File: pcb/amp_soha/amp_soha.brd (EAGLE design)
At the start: 90.2 x 48.9 mm, 59 parts, among them IC1 NE5535U, IC2 7812, IC3 7912, Q1 J113, Q2 J113, Q3 J113, Q4 J113

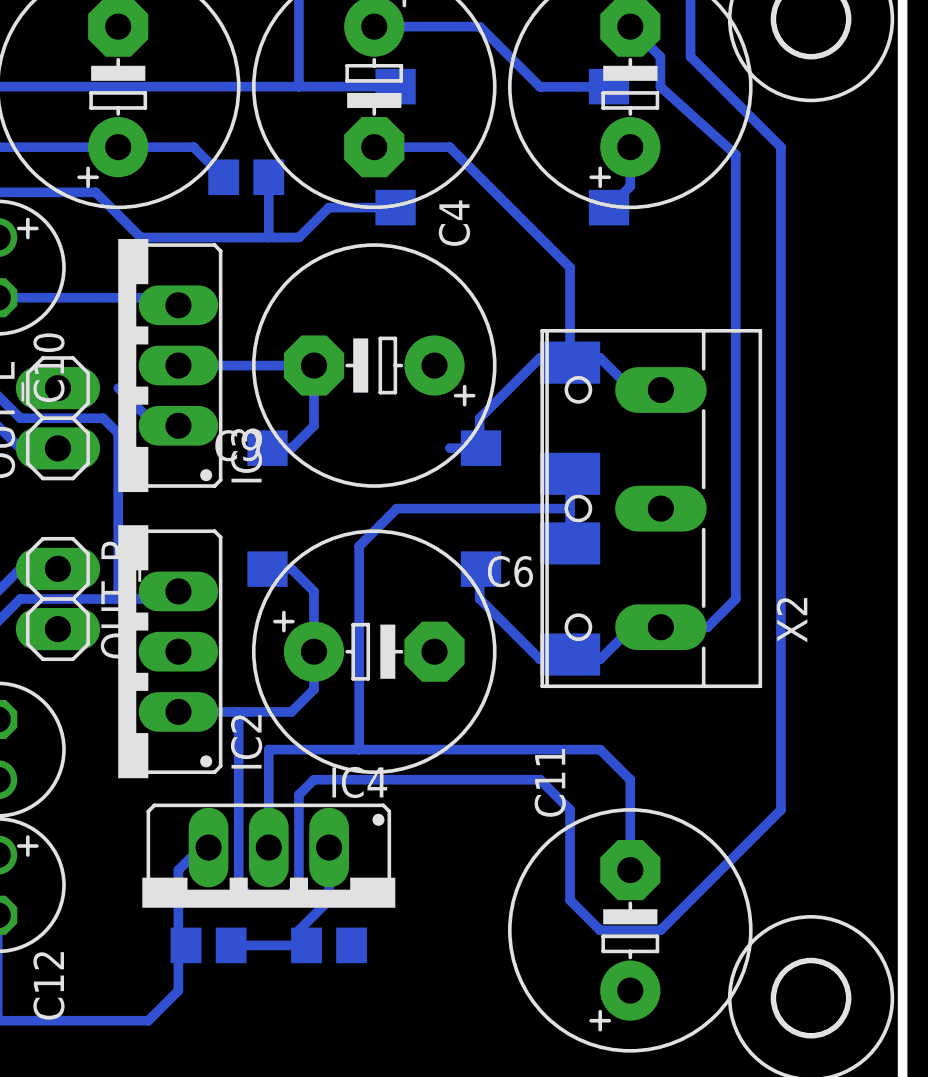
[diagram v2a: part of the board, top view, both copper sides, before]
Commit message: 
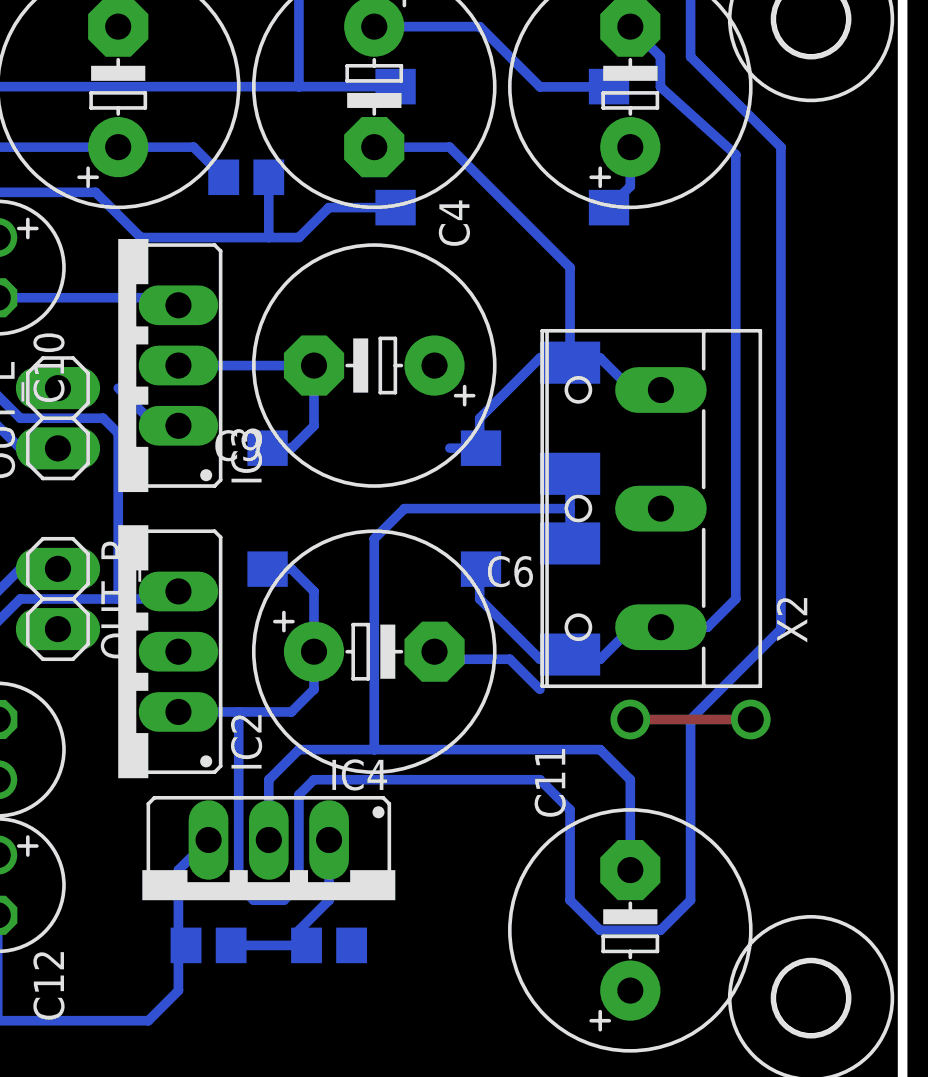
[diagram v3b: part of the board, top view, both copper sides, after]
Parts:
- moved IC4 0.32 mm to (63.5, 8.89)
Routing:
- net AGND: track 3.20 -> 13.3 mm, vias 0 -> 2
- net N$3: track 44.8 -> 43.2 mm
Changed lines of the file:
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@@
 <element name="R13" library="amp_soha" package="R0805" value="150" x="50.8" y="22.86" rot="MR270"/>
 <element name="OUT_R" library="amp_soha" package="1X02" value="" x="54.61" y="21.59" rot="R270"/>
-<element name="IC4" library="amp_soha" package="337TS" value="" x="63.5" y="8.5725" rot="R180"/>
+<element name="IC4" library="amp_soha" package="337TS" value="" x="63.5" y="8.89" rot="R180"/>
 <element name="R19" library="amp_soha" package="RTRIM3296Y" value="" x="10.16" y="9.8425"/>
 <element name="R18" library="amp_soha" package="RTRIM3296Y" value="" x="10.16" y="40.9575"/>
@@
 <wire x1="59.69" y1="28.8925" x2="58.7375" y2="28.8925" width="0.4064" layer="16"/>
 <wire x1="58.7375" y1="28.8925" x2="57.15" y2="30.48" width="0.4064" layer="16"/>
-<wire x1="57.15" y1="45.72" x2="52.07" y2="36.83" width="0" layer="19" extent="1-1"/>
+<wire x1="73.66" y1="19.05" x2="74.93" y2="17.78" width="0.4064" layer="16"/>
+<wire x1="71.12" y1="19.05" x2="73.66" y2="19.05" width="0.4064" layer="16"/>
+<wire x1="71.12" y1="19.05" x2="70.485" y2="19.3675" width="0.4064" layer="16"/>
+<via x="78.74" y="16.51" extent="1-16" drill="1.1" diameter="1.6764"/>
+<wire x1="78.74" y1="16.51" x2="83.82" y2="16.51" width="0.4064" layer="1"/>
+<via x="83.82" y="16.51" extent="1-16" drill="1.1" diameter="1.6764"/>
 </signal>
 <signal name="N$1">
@@
 <wire x1="76.2" y1="25.4" x2="76.2" y2="23.9325" width="0.4064" layer="16"/>
 <wire x1="76.2" y1="26.8675" x2="76.2" y2="25.4" width="0.4064" layer="16"/>
-<wire x1="76.2" y1="25.4" x2="68.8975" y2="25.4" width="0.4064" layer="16"/>
-<wire x1="68.8975" y1="25.4" x2="67.31" y2="23.8125" width="0.4064" layer="16"/>
-<wire x1="67.31" y1="23.8125" x2="67.31" y2="15.24" width="0.4064" layer="16"/>
-<wire x1="63.5" y1="11.1125" x2="63.5" y2="15.24" width="0.4064" layer="16"/>
-<wire x1="63.5" y1="15.24" x2="67.31" y2="15.24" width="0.4064" layer="16"/>
-<wire x1="67.31" y1="15.24" x2="77.47" y2="15.24" width="0.4064" layer="16"/>
+<wire x1="76.2" y1="25.4" x2="69.215" y2="25.4" width="0.4064" layer="16"/>
+<wire x1="69.215" y1="25.4" x2="67.945" y2="24.13" width="0.4064" layer="16"/>
+<wire x1="67.945" y1="24.13" x2="67.945" y2="15.24" width="0.4064" layer="16"/>
+<wire x1="67.945" y1="15.24" x2="77.47" y2="15.24" width="0.4064" layer="16"/>
 <wire x1="78.74" y1="10.16" x2="78.74" y2="13.97" width="0.4064" layer="16"/>
 <wire x1="78.74" y1="13.97" x2="77.47" y2="15.24" width="0.4064" layer="16"/>
+<wire x1="63.5" y1="11.43" x2="63.5" y2="13.97" width="0.4064" layer="16"/>
+<wire x1="63.5" y1="13.97" x2="64.77" y2="15.24" width="0.4064" layer="16"/>
+<wire x1="64.77" y1="15.24" x2="67.945" y2="15.24" width="0.4064" layer="16"/>
 </signal>
 <signal name="N$4">
@@
 <contactref element="IC4" pad="1"/>
 <wire x1="61.91" y1="6.985" x2="65.09" y2="6.985" width="0.4064" layer="16"/>
-<wire x1="66.04" y1="11.1125" x2="66.04" y2="8.89" width="0.4064" layer="16"/>
+<wire x1="66.04" y1="11.43" x2="66.04" y2="8.89" width="0.4064" layer="16"/>
 <wire x1="66.04" y1="8.89" x2="64.77" y2="7.62" width="0.4064" layer="16"/>
 <wire x1="64.77" y1="7.62" x2="64.77" y2="7.305" width="0.4064" layer="16"/>
@@
 <wire x1="59.69" y1="6.665" x2="60.01" y2="6.985" width="0.4064" layer="16"/>
 <wire x1="52.07" y1="8.255" x2="52.07" y2="3.81" width="0.4064" layer="16"/>
-<wire x1="60.96" y1="11.1125" x2="60.6425" y2="11.1125" width="0.4064" layer="16"/>
-<wire x1="60.6425" y1="11.1125" x2="59.69" y2="10.16" width="0.4064" layer="16"/>
+<wire x1="60.96" y1="11.43" x2="59.69" y2="10.16" width="0.4064" layer="16"/>
 <wire x1="59.69" y1="10.16" x2="59.69" y2="7.305" width="0.4064" layer="16"/>
 <wire x1="59.69" y1="7.305" x2="60.01" y2="6.985" width="0.4064" layer="16"/>
@@
 <wire x1="48.26" y1="45.72" x2="46.355" y2="45.72" width="0.4064" layer="16"/>
 <wire x1="77.47" y1="7.62" x2="80.01" y2="7.62" width="0.4064" layer="16"/>
-<wire x1="80.01" y1="7.62" x2="85.09" y2="12.7" width="0.4064" layer="16"/>
-<wire x1="85.09" y1="12.7" x2="85.09" y2="40.64" width="0.4064" layer="16"/>
+<wire x1="85.09" y1="20.32" x2="85.09" y2="40.64" width="0.4064" layer="16"/>
 <wire x1="85.09" y1="40.64" x2="81.28" y2="44.45" width="0.4064" layer="16"/>
 <wire x1="81.28" y1="44.45" x2="81.28" y2="46.99" width="0.4064" layer="16"/>
@@
 <wire x1="76.2" y1="12.7" x2="76.2" y2="8.89" width="0.4064" layer="16"/>
 <wire x1="76.2" y1="8.89" x2="77.47" y2="7.62" width="0.4064" layer="16"/>
+<wire x1="80.01" y1="7.62" x2="81.28" y2="8.89" width="0.4064" layer="16"/>
+<wire x1="81.28" y1="8.89" x2="81.28" y2="16.51" width="0.4064" layer="16"/>
+<wire x1="81.28" y1="16.51" x2="85.09" y2="20.32" width="0.4064" layer="16"/>
 </signal>
 <signal name="N$10">

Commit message: 
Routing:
- net AGND: track 13.3 -> 8.28 mm
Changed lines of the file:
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@@
 <wire x1="59.69" y1="28.8925" x2="58.7375" y2="28.8925" width="0.4064" layer="16"/>
 <wire x1="58.7375" y1="28.8925" x2="57.15" y2="30.48" width="0.4064" layer="16"/>
-<wire x1="73.66" y1="19.05" x2="74.93" y2="17.78" width="0.4064" layer="16"/>
-<wire x1="71.12" y1="19.05" x2="73.66" y2="19.05" width="0.4064" layer="16"/>
-<wire x1="71.12" y1="19.05" x2="70.485" y2="19.3675" width="0.4064" layer="16"/>
 <via x="78.74" y="16.51" extent="1-16" drill="1.1" diameter="1.6764"/>
 <wire x1="78.74" y1="16.51" x2="83.82" y2="16.51" width="0.4064" layer="1"/>
